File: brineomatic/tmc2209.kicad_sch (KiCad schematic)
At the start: 17 parts, among them J21 Conn_01x04, U9 TMC2209-LA

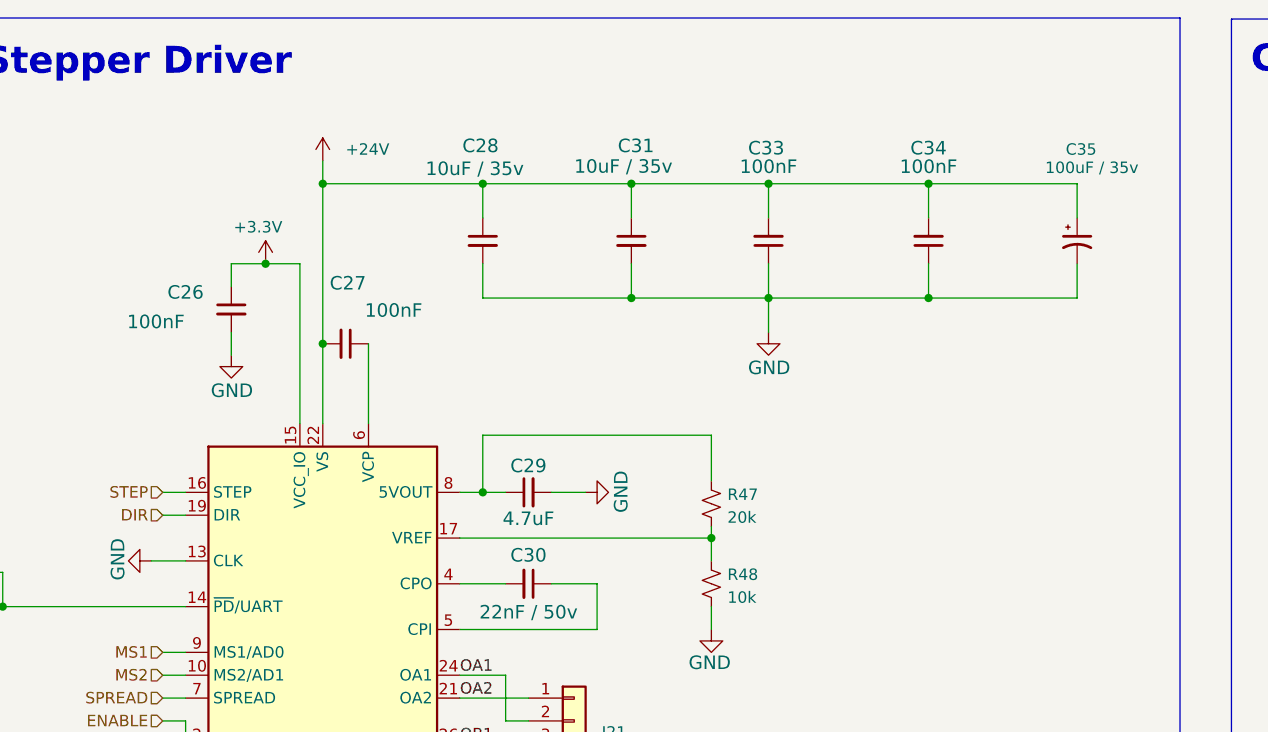
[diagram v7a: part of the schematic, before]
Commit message: added esd protection to relay driver connector
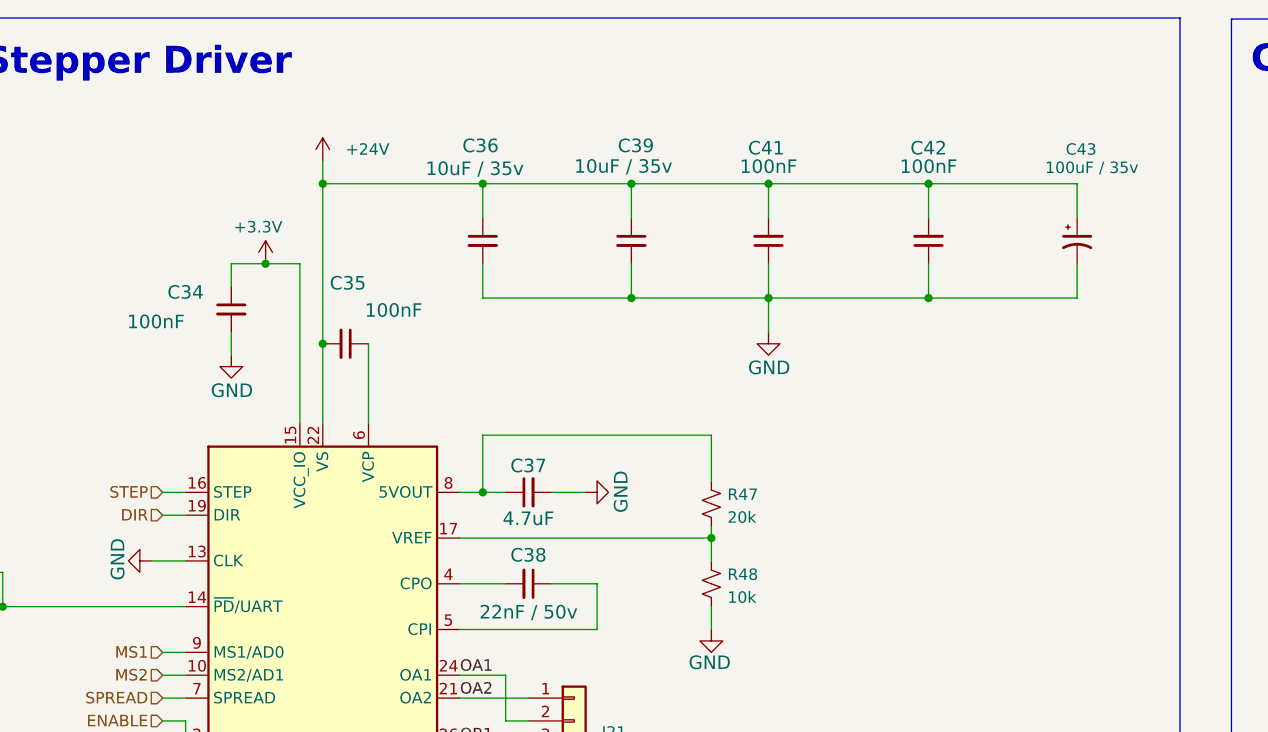
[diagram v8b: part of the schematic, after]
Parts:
- renumbered C26 to C34, C27 to C35, C28 to C36, C29 to C37, C30 to C38, C31 to C39, C33 to C41, C34 to C42, C35 to C43
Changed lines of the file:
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@@
 		(on_board yes)
 		(dnp no)
-		(property "Reference" "C31"
+		(property "Reference" "C39"
 			(at 118.11 45.72 0)
 			(effects
@@
 			(project "brineomatic"
 				(path "/96477ae2-ef08-48f3-8dd4-fe4478541f68/0f01c39f-0c25-414e-9ed3-1ba09e2af0c5"
-					(reference "C31")
+					(reference "C39")
 					(unit 1)
 				)
@@
 		(on_board yes)
 		(dnp no)
-		(property "Reference" "C34"
+		(property "Reference" "C42"
 			(at 148.59 45.974 0)
 			(effects
@@
 			(project "brineomatic"
 				(path "/96477ae2-ef08-48f3-8dd4-fe4478541f68/0f01c39f-0c25-414e-9ed3-1ba09e2af0c5"
-					(reference "C34")
+					(reference "C42")
 					(unit 1)
 				)
@@
 		(on_board yes)
 		(dnp no)
-		(property "Reference" "C27"
+		(property "Reference" "C35"
 			(at 84.074 62.738 90)
 			(effects
@@
 			(project "brineomatic"
 				(path "/96477ae2-ef08-48f3-8dd4-fe4478541f68/0f01c39f-0c25-414e-9ed3-1ba09e2af0c5"
-					(reference "C27")
+					(reference "C35")
 					(unit 1)
 				)
@@
 		(on_board yes)
 		(dnp no)
-		(property "Reference" "C35"
+		(property "Reference" "C43"
 			(at 163.83 46.99 0)
 			(effects
@@
 			(project ""
 				(path "/96477ae2-ef08-48f3-8dd4-fe4478541f68/0f01c39f-0c25-414e-9ed3-1ba09e2af0c5"
-					(reference "C35")
+					(reference "C43")
 					(unit 1)
 				)
@@
 		(on_board yes)
 		(dnp no)
-		(property "Reference" "C28"
+		(property "Reference" "C36"
 			(at 100.838 45.72 0)
 			(effects
@@
 			(project "brineomatic"
 				(path "/96477ae2-ef08-48f3-8dd4-fe4478541f68/0f01c39f-0c25-414e-9ed3-1ba09e2af0c5"
-					(reference "C28")
+					(reference "C36")
 					(unit 1)
 				)
@@
 		(on_board yes)
 		(dnp no)
-		(property "Reference" "C26"
+		(property "Reference" "C34"
 			(at 66.04 63.754 0)
 			(effects
@@
 			(project "brineomatic"
 				(path "/96477ae2-ef08-48f3-8dd4-fe4478541f68/0f01c39f-0c25-414e-9ed3-1ba09e2af0c5"
-					(reference "C26")
+					(reference "C34")
 					(unit 1)
 				)
@@
 		(on_board yes)
 		(dnp no)
-		(property "Reference" "C30"
+		(property "Reference" "C38"
 			(at 104.14 92.964 90)
 			(effects
@@
 			(project "brineomatic"
 				(path "/96477ae2-ef08-48f3-8dd4-fe4478541f68/0f01c39f-0c25-414e-9ed3-1ba09e2af0c5"
-					(reference "C30")
+					(reference "C38")
 					(unit 1)
 				)
@@
 		(on_board yes)
 		(dnp no)
-		(property "Reference" "C29"
+		(property "Reference" "C37"
 			(at 104.14 81.28 90)
 			(effects
@@
 			(project "brineomatic"
 				(path "/96477ae2-ef08-48f3-8dd4-fe4478541f68/0f01c39f-0c25-414e-9ed3-1ba09e2af0c5"
-					(reference "C29")
+					(reference "C37")
 					(unit 1)
 				)
@@
 		(on_board yes)
 		(dnp no)
-		(property "Reference" "C33"
+		(property "Reference" "C41"
 			(at 130.556 45.974 0)
 			(effects
@@
 			(project "brineomatic"
 				(path "/96477ae2-ef08-48f3-8dd4-fe4478541f68/0f01c39f-0c25-414e-9ed3-1ba09e2af0c5"
-					(reference "C33")
-					(unit 1)
-				)
+					(reference "C41")
+					(unit 1)
+				)
